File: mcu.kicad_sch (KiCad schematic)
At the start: 32 parts, among them J2 Conn_01x10, J3 Conn_01x10, J4 Conn_02x05_Odd_Even, U5 REF3033, U7 STM32F407VGTx, Y1 8MHz

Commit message: sch: Correct SWD Header MF/PN and Update Footprint - Use Adafuit 4048 Mini SWD Headers - Silkscreen is modified to indicate orientation of the header
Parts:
- J4: footprint Connector_PinHeader_1.27mm:PinHeader_2x05_P1.27mm_Vertical_SMD -> kirdy:Adafuit_SWD_Header_4048; MFR_PN M50-3600542 -> 4048
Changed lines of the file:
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@@
       (effects (font (size 1.27 1.27)))
     )
-    (property "Footprint" "Connector_PinHeader_1.27mm:PinHeader_2x05_P1.27mm_Vertical_SMD" (at 317.5 91.44 0)
+    (property "Footprint" "kirdy:Adafuit_SWD_Header_4048" (at 317.5 91.44 0)
       (effects (font (size 1.27 1.27)) hide)
     )
-    (property "Datasheet" "~" (at 317.5 91.44 0)
+    (property "Datasheet" "https://www.mouser.hk/datasheet/2/737/Adafruit_4048_Web-3358014.pdf" (at 317.5 91.44 0)
       (effects (font (size 1.27 1.27)) hide)
     )
-    (property "MFR_PN" "M50-3600542" (at 317.5 91.44 0)
+    (property "MFR_PN" "4048" (at 317.5 91.44 0)
       (effects (font (size 1.27 1.27)) hide)
     )

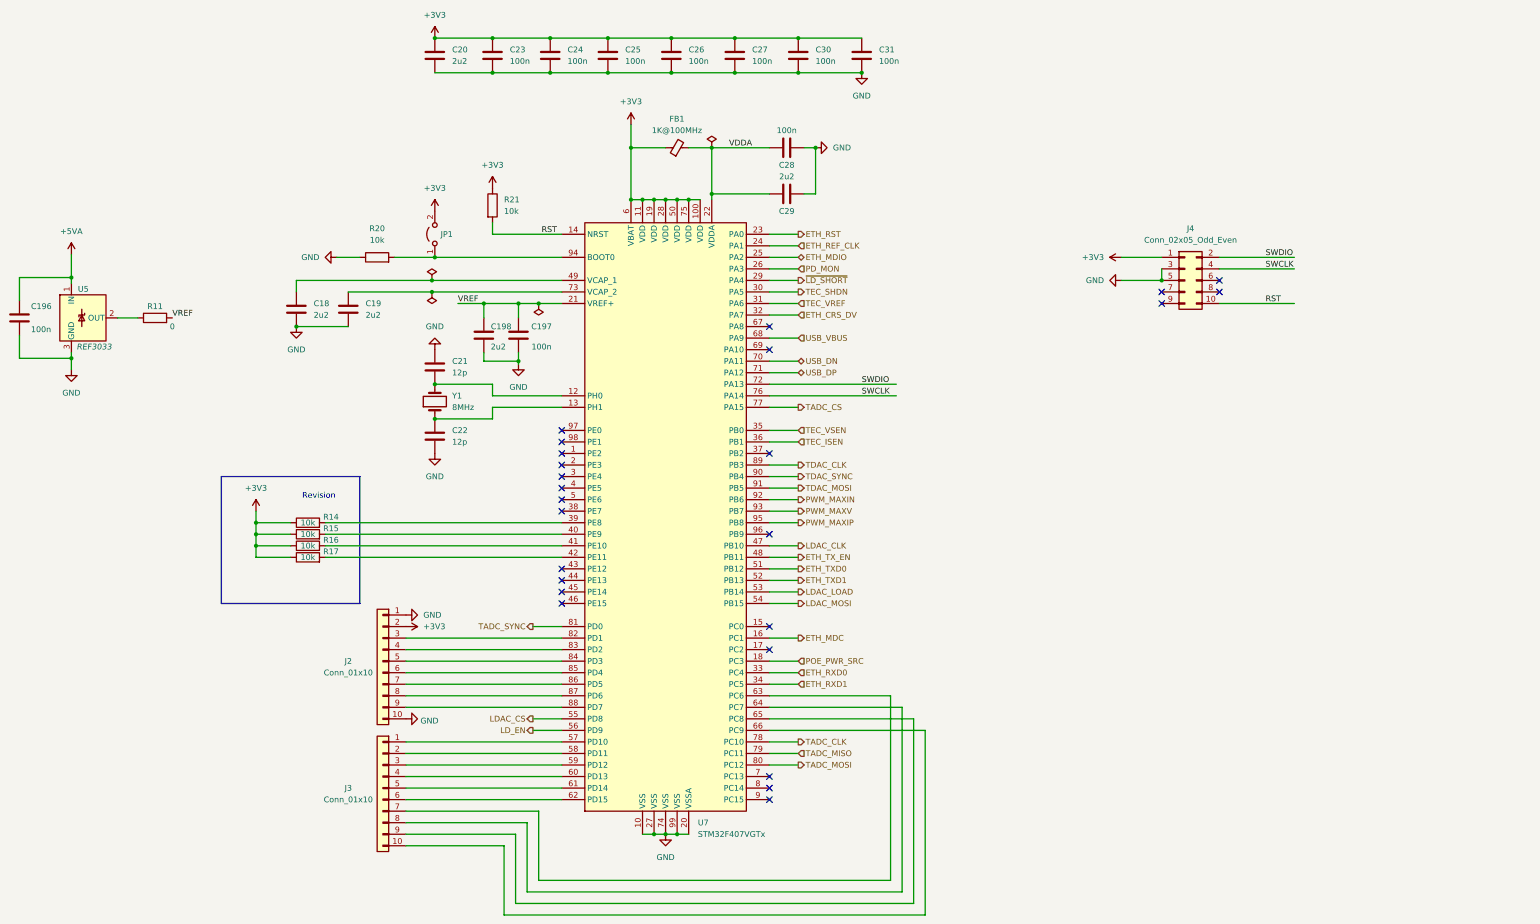
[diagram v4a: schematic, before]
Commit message: sch: Add redundant 2.54mm SWD Header
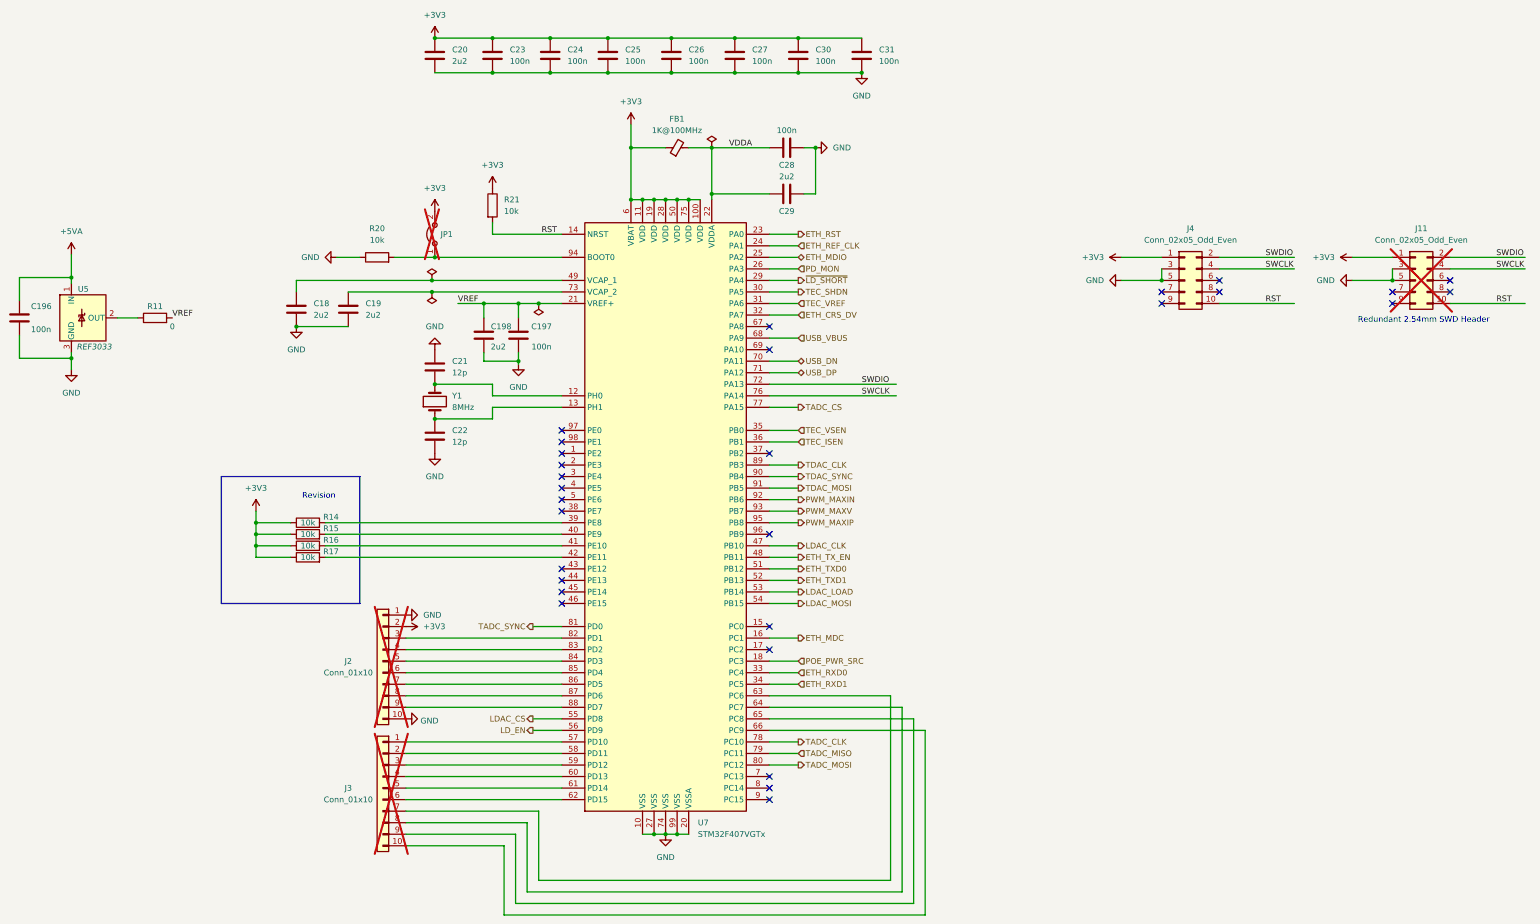
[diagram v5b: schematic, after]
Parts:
- added J11: Conn_02x05_Odd_Even, Connector_PinHeader_2.54mm:PinHeader_2x05_P2.54mm_Vertical, symbol Connector_Generic:Conn_02x05_Odd_Even
- J2, J3, JP1: now not fitted
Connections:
- net +3V3: now also J11.1 (Pin_1)
- net GND: now also J11.3 (Pin_3), J11.5 (Pin_5)
- net RST: now also J11.10 (Pin_10)
- net SWCLK: now also J11.4 (Pin_4)
- net SWDIO: now also J11.2 (Pin_2)
- no-connect marks 25 -> 29
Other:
- note added: "Redundant 2.54mm SWD Header"
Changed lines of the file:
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@@
   (junction (at 236.22 62.23) (diameter 0) (color 0 0 0 0)
+  )
+  (junction (at 363.22 91.44) (diameter 0) (color 0 0 0 0)
   )
   (junction (at 152.4 38.1) (diameter 0) (color 0 0 0 0)
@@
   (no_connect (at 325.12 93.98))
   (no_connect (at 325.12 91.44))
+  (no_connect (at 375.92 93.98))
   (no_connect (at 180.34 157.48))
   (no_connect (at 180.34 154.94))
+  (no_connect (at 375.92 91.44))
   (no_connect (at 312.42 93.98))
+  (no_connect (at 363.22 96.52))
   (no_connect (at 226.06 172.72))
+  (no_connect (at 363.22 93.98))
   (no_connect (at 226.06 101.6))
   (no_connect (at 226.06 200.66))
@@
     (stroke (width 0) (type default))
   )
+  (wire (pts (xy 375.92 86.36) (xy 392.43 86.36))
+    (stroke (width 0) (type default))
+  )
   (wire (pts (xy 172.72 226.06) (xy 172.72 210.82))
     (stroke (width 0) (type default))
@@
     (stroke (width 0) (type default))
   )
+  (wire (pts (xy 354.33 86.36) (xy 363.22 86.36))
+    (stroke (width 0) (type default))
+  )
   (wire (pts (xy 165.1 119.38) (xy 165.1 121.92))
     (stroke (width 0) (type default))
@@
     (stroke (width 0) (type default))
   )
+  (wire (pts (xy 375.92 88.9) (xy 392.43 88.9))
+    (stroke (width 0) (type default))
+  )
   (wire (pts (xy 232.41 38.1) (xy 246.38 38.1))
     (stroke (width 0) (type default))
@@
     (stroke (width 0) (type default))
   )
+  (wire (pts (xy 375.92 96.52) (xy 392.43 96.52))
+    (stroke (width 0) (type default))
+  )
   (wire (pts (xy 163.195 96.52) (xy 170.815 96.52))
     (stroke (width 0) (type default))
@@
     (stroke (width 0) (type default))
   )
+  (wire (pts (xy 363.22 88.9) (xy 363.22 91.44))
+    (stroke (width 0) (type default))
+  )
   (wire (pts (xy 152.4 38.1) (xy 165.1 38.1))
     (stroke (width 0) (type default))
@@
     (stroke (width 0) (type default))
   )
+  (wire (pts (xy 354.33 91.44) (xy 363.22 91.44))
+    (stroke (width 0) (type default))
+  )
   (wire (pts (xy 128.27 152.4) (xy 180.34 152.4))
     (stroke (width 0) (type default))
@@
   (wire (pts (xy 200.66 73.66) (xy 203.2 73.66))
     (stroke (width 0) (type default))
+  )
+  (text "Redundant 2.54mm SWD Header" (at 355.6 100.965 0)
+    (effects (font (size 1.27 1.27)) (justify left bottom))
   )
   (text "Revision\n" (at 123.19 139.7 0)
@@
     (effects (font (size 1.27 1.27)) (justify left bottom))
   )
+  (label "SWCLK" (at 386.08 88.9 0) (fields_autoplaced)
+    (effects (font (size 1.27 1.27)) (justify left bottom))
+  )
+  (label "RST" (at 386.08 96.52 0) (fields_autoplaced)
+    (effects (font (size 1.27 1.27)) (justify left bottom))
+  )
   (label "SWDIO" (at 335.28 86.36 0) (fields_autoplaced)
     (effects (font (size 1.27 1.27)) (justify left bottom))
   )
   (label "VREF" (at 157.48 96.52 0) (fields_autoplaced)
+    (effects (font (size 1.27 1.27)) (justify left bottom))
+  )
+  (label "SWDIO" (at 386.08 86.36 0) (fields_autoplaced)
     (effects (font (size 1.27 1.27)) (justify left bottom))
   )
@@
   )
   (symbol (lib_id "Connector_Generic:Conn_01x10") (at 140.97 175.26 0) (mirror y) (unit 1)
-    (in_bom yes) (on_board yes) (dnp no)
+    (in_bom yes) (on_board yes) (dnp yes)
     (property "Reference" "J2" (at 133.35 175.26 0)
       (effects (font (size 1.27 1.27)))
@@
   )
   (symbol (lib_id "Jumper:Jumper_2_Open") (at 152.4 81.28 90) (unit 1)
-    (in_bom yes) (on_board yes) (dnp no)
+    (in_bom yes) (on_board yes) (dnp yes)
     (property "Reference" "JP1" (at 153.67 81.28 90)
       (effects (font (size 1.27 1.27)) (justify right))
@@
         (path "/88da1dd8-9274-4b55-84fb-90006c9b6e8f/e9afb2cc-7f7f-4cb9-888a-0bfd71b1d070"
           (reference "#FLG04") (unit 1)
+        )
+      )
+    )
+  )
+  (symbol (lib_id "Connector_Generic:Conn_02x05_Odd_Even") (at 368.3 91.44 0) (unit 1)
+    (in_bom yes) (on_board yes) (dnp yes) (fields_autoplaced)
+    (property "Reference" "J11" (at 369.57 80.01 0)
+      (effects (font (size 1.27 1.27)))
+    )
+    (property "Value" "Conn_02x05_Odd_Even" (at 369.57 82.55 0)
+      (effects (font (size 1.27 1.27)))
+    )
+    (property "Footprint" "Connector_PinHeader_2.54mm:PinHeader_2x05_P2.54mm_Vertical" (at 368.3 91.44 0)
+      (effects (font (size 1.27 1.27)) hide)
+    )
+    (property "Datasheet" "" (at 368.3 91.44 0)
+      (effects (font (size 1.27 1.27)) hide)
+    )
+    (property "MFR_PN" "" (at 368.3 91.44 0)
+      (effects (font (size 1.27 1.27)) hide)
+    )
+    (pin "1")
+    (pin "10")
+    (pin "2")
+    (pin "3")
+    (pin "4")
+    (pin "5")
+    (pin "6")
+    (pin "7")
+    (pin "8")
+    (pin "9")
+    (instances
+      (project "kirdy"
+        (path "/88da1dd8-9274-4b55-84fb-90006c9b6e8f/e9afb2cc-7f7f-4cb9-888a-0bfd71b1d070"
+          (reference "J11") (unit 1)
         )
       )
@@
     )
   )
+  (symbol (lib_id "power:GND") (at 354.33 91.44 270) (unit 1)
+    (in_bom yes) (on_board yes) (dnp no) (fields_autoplaced)
+    (property "Reference" "#PWR053" (at 347.98 91.44 0)
+      (effects (font (size 1.27 1.27)) hide)
+    )
+    (property "Value" "GND" (at 350.52 91.4399 90)
+      (effects (font (size 1.27 1.27)) (justify right))
+    )
+    (property "Footprint" "" (at 354.33 91.44 0)
+      (effects (font (size 1.27 1.27)) hide)
+    )
+    (property "Datasheet" "" (at 354.33 91.44 0)
+      (effects (font (size 1.27 1.27)) hide)
+    )
+    (pin "1")
+    (instances
+      (project "kirdy"
+        (path "/88da1dd8-9274-4b55-84fb-90006c9b6e8f/e9afb2cc-7f7f-4cb9-888a-0bfd71b1d070"
+          (reference "#PWR053") (unit 1)
+        )
+      )
+    )
+  )
   (symbol (lib_id "Device:C") (at 165.1 41.91 0) (unit 1)
     (in_bom yes) (on_board yes) (dnp no) (fields_autoplaced)
@@
     )
   )
+  (symbol (lib_id "power:+3V3") (at 354.33 86.36 90) (unit 1)
+    (in_bom yes) (on_board yes) (dnp no) (fields_autoplaced)
+    (property "Reference" "#PWR052" (at 358.14 86.36 0)
+      (effects (font (size 1.27 1.27)) hide)
+    )
+    (property "Value" "+3V3" (at 350.52 86.3599 90)
+      (effects (font (size 1.27 1.27)) (justify left))
+    )
+    (property "Footprint" "" (at 354.33 86.36 0)
+      (effects (font (size 1.27 1.27)) hide)
+    )
+    (property "Datasheet" "" (at 354.33 86.36 0)
+      (effects (font (size 1.27 1.27)) hide)
+    )
+    (pin "1")
+    (instances
+      (project "kirdy"
+        (path "/88da1dd8-9274-4b55-84fb-90006c9b6e8f/e9afb2cc-7f7f-4cb9-888a-0bfd71b1d070"
+          (reference "#PWR052") (unit 1)
+        )
+      )
+    )
+  )
   (symbol (lib_id "power:GND") (at 121.92 101.6 0) (unit 1)
     (in_bom yes) (on_board yes) (dnp no) (fields_autoplaced)
@@
   )
   (symbol (lib_id "Connector_Generic:Conn_01x10") (at 140.97 203.2 0) (mirror y) (unit 1)
-    (in_bom yes) (on_board yes) (dnp no)
+    (in_bom yes) (on_board yes) (dnp yes)
     (property "Reference" "J3" (at 133.35 203.2 0)
       (effects (font (size 1.27 1.27)))

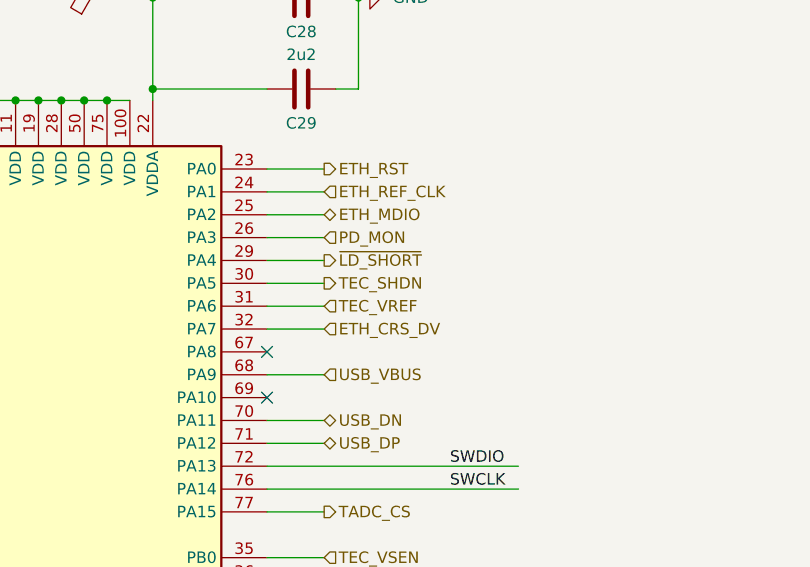
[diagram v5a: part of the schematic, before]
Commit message: sch: Correct typos in TEC_~{SHDN} ports
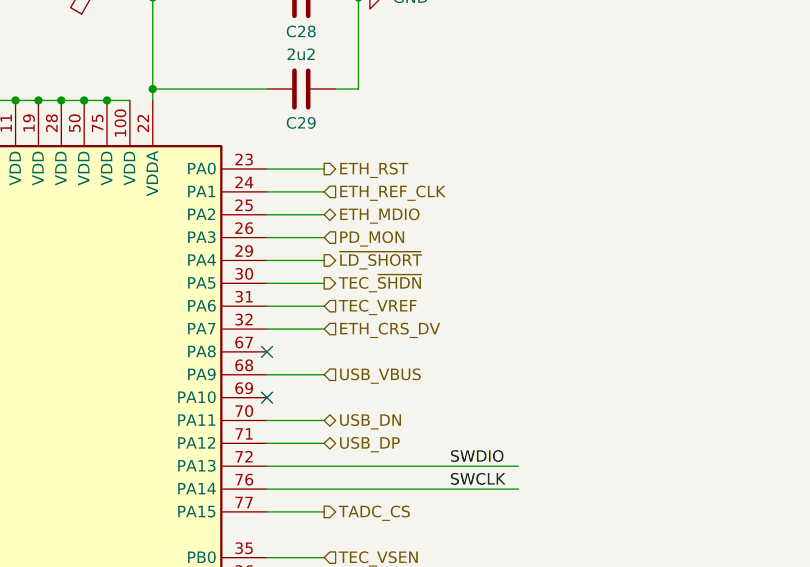
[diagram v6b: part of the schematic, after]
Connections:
- net TEC_SHDN renamed TEC_~{SHDN}
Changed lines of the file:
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@@
     (effects (font (size 1.27 1.27)) (justify left))
   )
-  (hierarchical_label "TEC_SHDN" (shape output) (at 232.41 93.98 0) (fields_autoplaced)
+  (hierarchical_label "TEC_~{SHDN}" (shape output) (at 232.41 93.98 0) (fields_autoplaced)
     (effects (font (size 1.27 1.27)) (justify left))
   )
